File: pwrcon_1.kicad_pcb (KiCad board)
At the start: 2 copper layers, 85.1 x 48 mm, 52 parts, among them J1 CON3, J4 CON3, J5 Conn_01x03_Female, J6 Conn_01x04, J7 CON3, J8 Conn_01x03_Female, Q1 Q_PNP_BEC, U1 LM358, U2 ISOW7841DWE, U3 THVD1500D, U4 SN74LV1T34DBVR, U5 SN74LV1T34DBVR, U6 SN74LV1T34DBVR, U7 MIC5219-3.3YMM

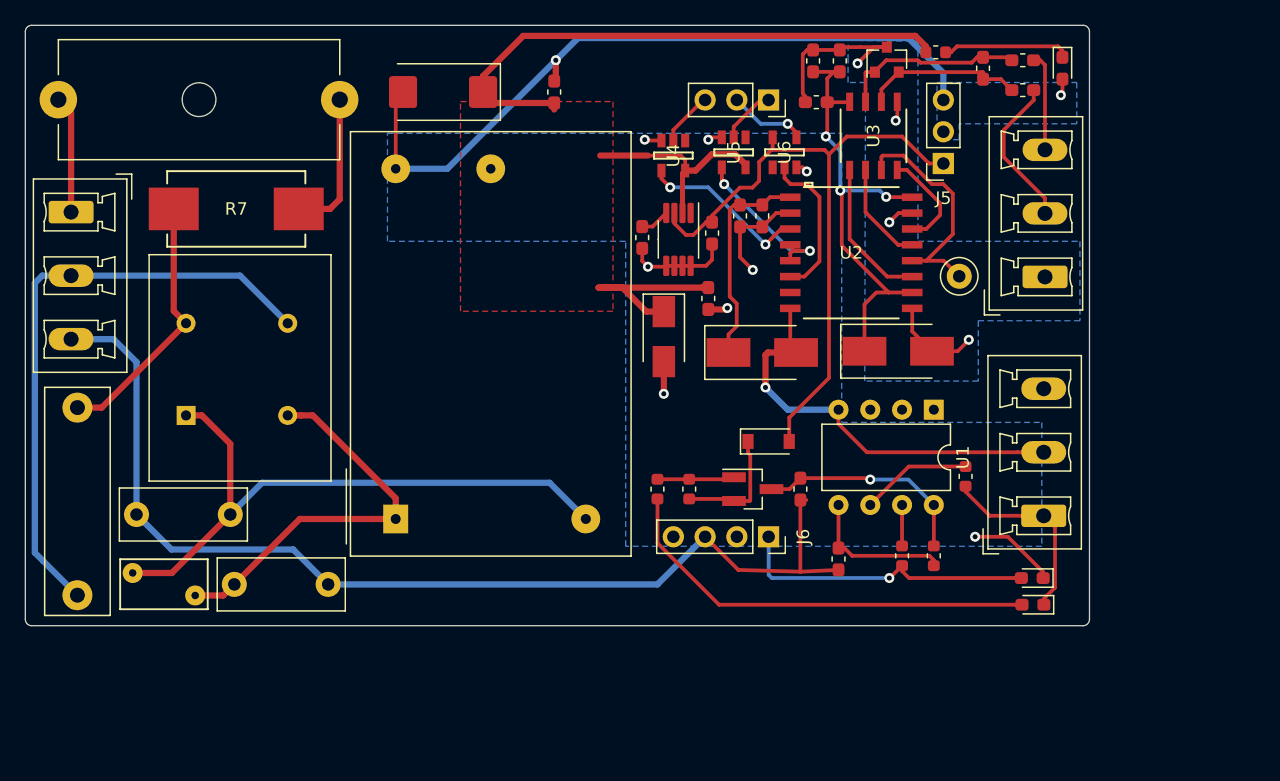
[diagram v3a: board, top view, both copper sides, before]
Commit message: More routing, component footprints finalised and missing ones added into repo
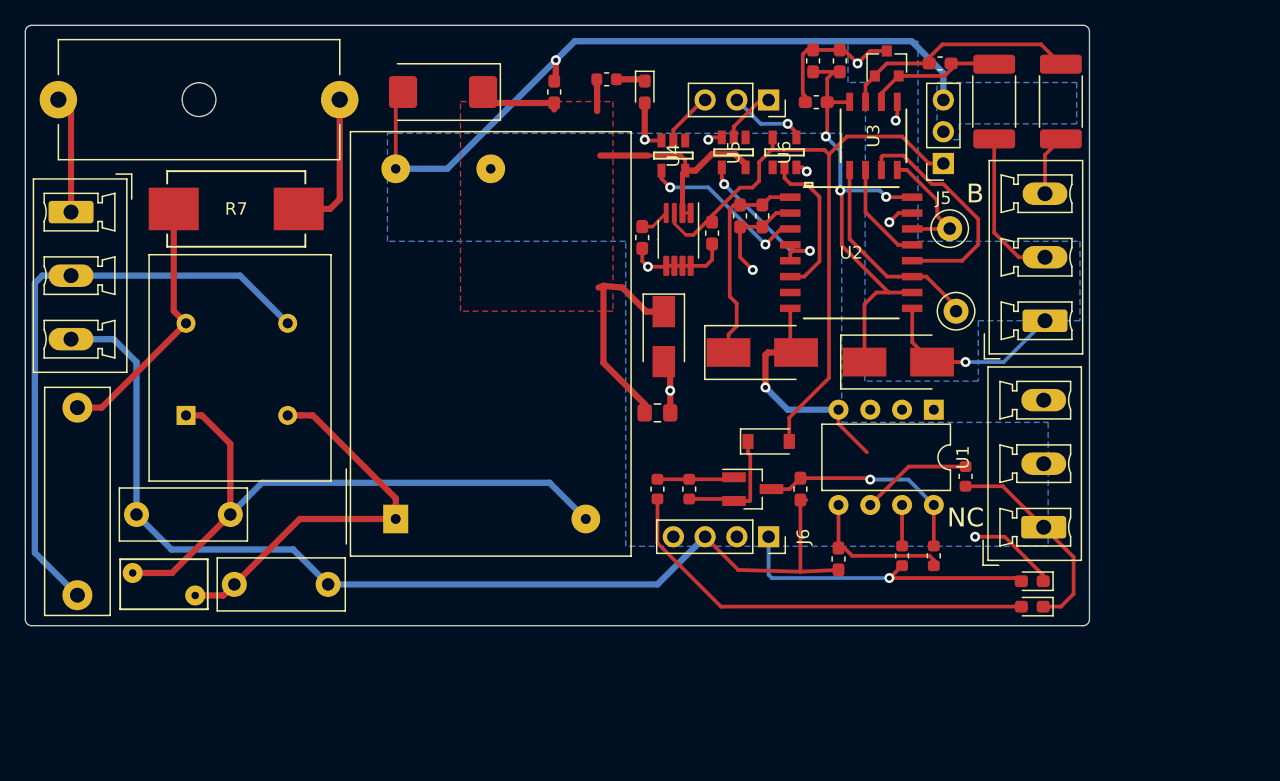
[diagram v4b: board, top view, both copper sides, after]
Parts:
- added TP5: TestPoint, TestPoint:TestPoint_Loop_D1.80mm_Drill1.0mm_Beaded, F.Cu at (175.8, 77.0)
- R10, R11: footprint Resistor_SMD:R_0603_1608Metric_Pad1.05x0.95mm_HandSolder -> Resistor_SMD:R_2512_6332Metric_Pad1.52x3.35mm_HandSolder
- R8: footprint Resistor_SMD:R_0603_1608Metric_Pad1.05x0.95mm_HandSolder -> Resistor_SMD:R_0805_2012Metric_Pad1.15x1.40mm_HandSolder
- moved DR2 33.5 mm to (151.4, 66.0)
- moved R9 26.4 mm to (148.3, 65.0)
- moved R8 10.0 mm to (152.4, 91.7), turned to 0 degrees
- moved R10 4.49 mm to (184.7, 66.8), turned to 90 degrees
- moved J7 3.51 mm to (183.4, 84.3)
- moved R12 3.45 mm to (175.0, 63.8), turned to 180 degrees
- moved TP4 2.81 mm to (176.3, 83.6)
- moved R11 2.46 mm to (179.3, 66.8), turned to 90 degrees
- moved J1 0.91 mm to (183.3, 100.8)
- moved D4 0.86 mm to (171.7, 87.6)
- moved D6 0.30 mm to (170.7, 63.8)
- moved DG1 0.25 mm to (182.4, 105.2)
- moved DR1 0.16 mm to (182.4, 107.2)
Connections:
- U2 pad 11: Net-(U2-Pad11) -> Net-(TP4-Pad1)
- U2 pad 12: Net-(TP4-Pad1) -> Net-(U2-Pad12)
- U3 pad 1: Net-(U2-Pad11) -> Net-(TP4-Pad1)
- U3 pad 3: Net-(TP4-Pad1) -> Net-(U2-Pad12)
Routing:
- net /5VDC: track 79.6 -> 46.3 mm
- net Net-(U2-Pad12): track 0.00 -> 18.8 mm
- net GND: track 212.0 -> 199.6 mm, vias 11 -> 9
- net Net-(U2-Pad11): track 11.8 -> 0.00 mm
- net Net-(DR2-Pad1): track 10.2 -> 2.32 mm
- net GNDA: track 24.9 -> 31.0 mm
- net Net-(D6-Pad1): track 14.8 -> 19.3 mm
- net Net-(J7-Pad3): track 7.84 -> 4.90 mm
- net Net-(TP4-Pad1): track 18.6 -> 16.7 mm
- net Net-(TP5-Pad1): track 8.17 -> 9.89 mm
- net Net-(D6-Pad2): track 12.9 -> 11.3 mm
- net /NC: track 15.3 -> 16.8 mm
- net Net-(DG1-Pad2): track 24.4 -> 25.4 mm
- net Net-(C4-Pad2): track 38.3 -> 39.2 mm
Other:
- board text added: "B"
- board text added: "NC"

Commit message: Aisler fab submit
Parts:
- moved J8 9.01 mm to (152.3, 67.7), turned to 90 degrees
- moved J6 8.95 mm to (152.3, 101.7), turned to 90 degrees
- moved D5 2.64 mm to (158.2, 86.4), turned to 270 degrees
- moved DR2 2.43 mm to (149.4, 64.7)
- moved R9 1.61 mm to (146.7, 64.8), turned to 270 degrees
- moved U5 0.89 mm to (158.5, 71.8)
- moved U4 0.85 mm to (153.9, 71.9)
- moved U6 0.83 mm to (162.6, 71.7)
- moved U2 0.74 mm to (167.9, 79.6)
- moved C7 0.64 mm to (160.8, 76.6)
- moved C8 0.64 mm to (159.0, 76.6)
- moved C10 0.57 mm to (156.8, 77.9)
- moved C11 0.57 mm to (151.2, 78.2)
- moved U7 0.57 mm to (154.1, 78.4)
- moved C2 0.38 mm to (118.6, 105.8)
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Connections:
- J6 pad 3: GND -> (no net)
- J8 pad 2: /RS485_RXD -> /RS485_TXD
- J8 pad 3: /RS485_TXD -> /RS485_RXD
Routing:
- net /RS485_EN: track 4.53 -> 12.9 mm
- net Net-(DG1-Pad2): track 25.4 -> 33.0 mm, vias 1 -> 0
- net /5VDC: track 46.3 -> 53.2 mm
- net Net-(DR1-Pad2): track 34.7 -> 41.0 mm
- net Net-(C2-Pad1): track 31.6 -> 27.2 mm
- net Net-(C7-Pad1): track 17.2 -> 13.1 mm
- net GND: track 199.6 -> 195.9 mm
- net /RS485_RXD: track 6.23 -> 8.04 mm
- net Net-(F1-Pad2): track 11.6 -> 10.0 mm
- net /RS485_TXD: track 4.38 -> 3.48 mm
- net Net-(U2-Pad13): track 8.19 -> 9.01 mm
- net GNDA: track 31.0 -> 30.4 mm
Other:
- board text added: "3V3"
- board text added: "ANA_IN3"
- board text added: "L"
- board text added: "RX"
- board text added: "TX"

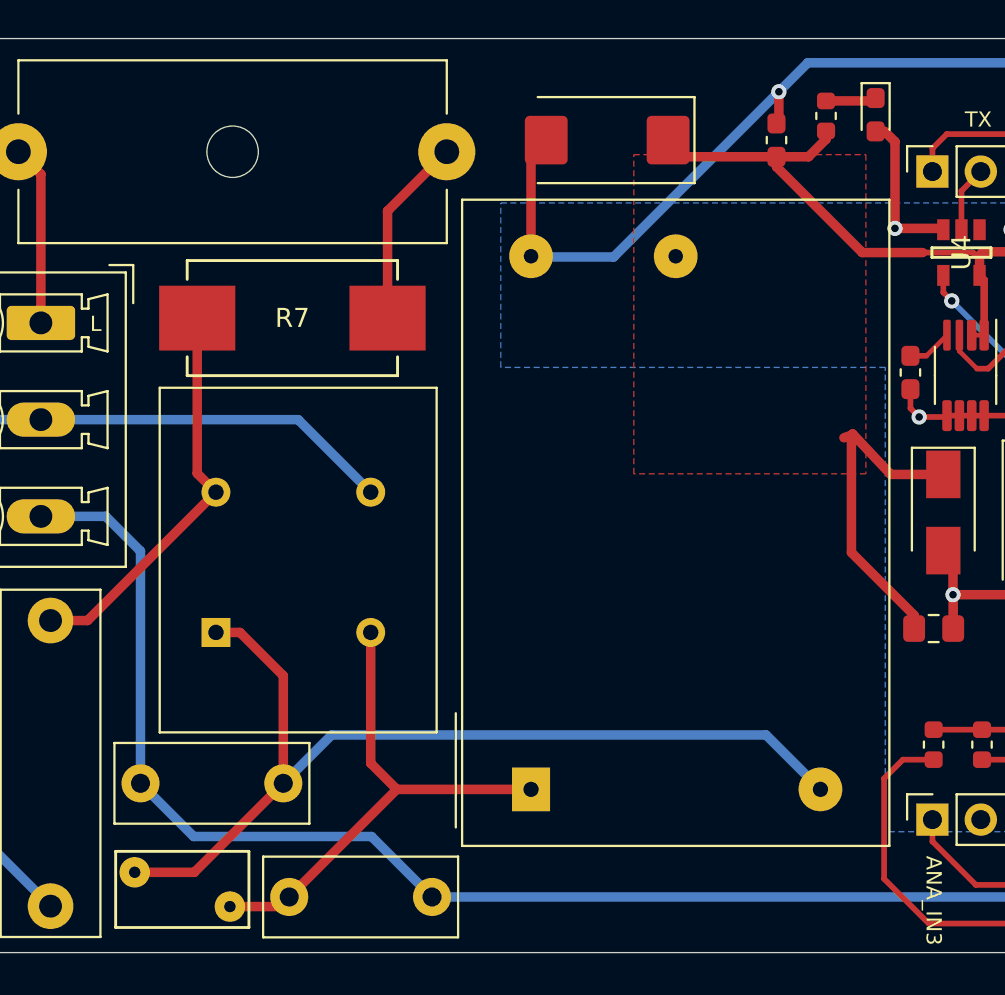
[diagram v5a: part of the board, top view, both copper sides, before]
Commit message: Flipped varistor and led in schematic (no difference to board), cleaned up project/global footprint libraries
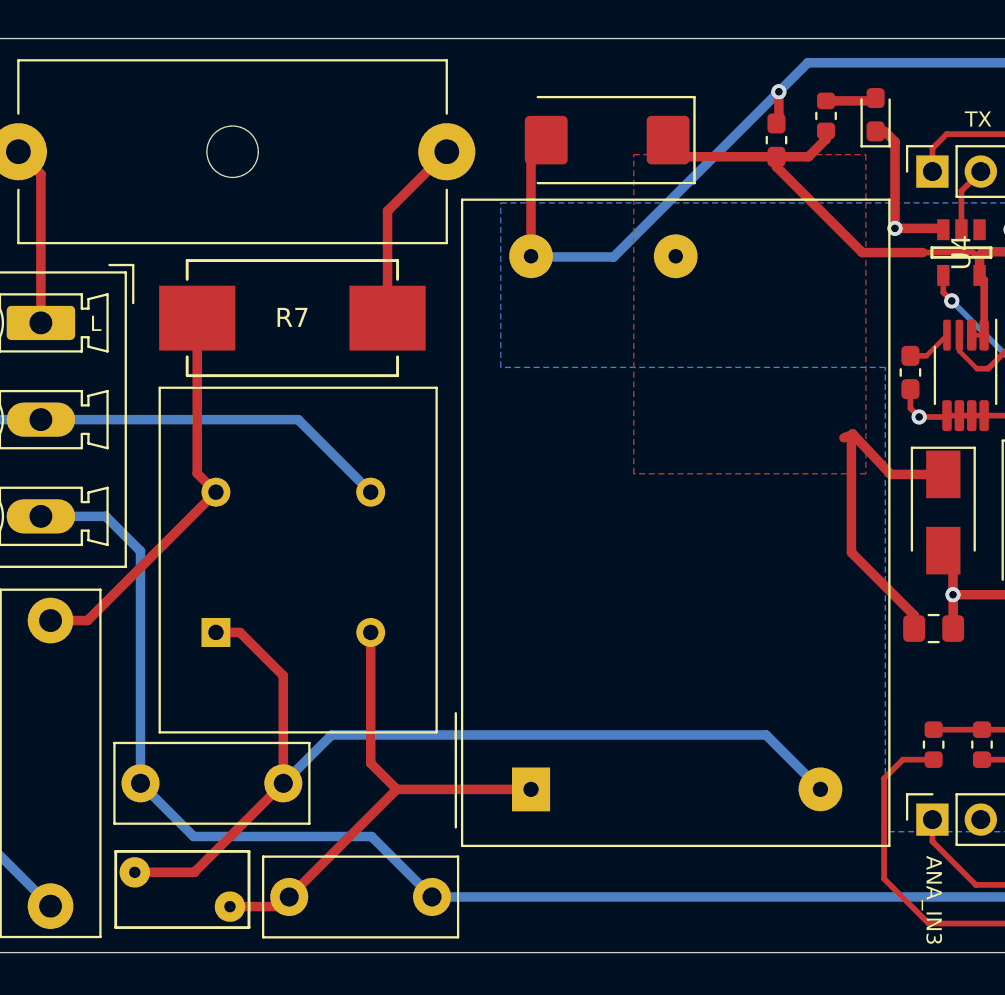
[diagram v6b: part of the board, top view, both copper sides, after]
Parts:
- moved RV1 5.32 mm to (115.4, 106.3), turned to 180 degrees
- turned DR2 to 90 degrees
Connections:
- DR2 pad 1: Net-(DR2-Pad1) -> GND
- DR2 pad 2: GND -> Net-(DR2-Pad2)
- R9 pad 1: Net-(DR2-Pad1) -> Net-(DR2-Pad2)
- RV1 pad 1: Net-(C1-Pad2) -> Net-(C2-Pad1)
- RV1 pad 2: Net-(C2-Pad1) -> Net-(C1-Pad2)
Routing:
- net Net-(DR2-Pad2): track 0.00 -> 2.67 mm
- net Net-(DR2-Pad1): track 2.67 -> 0.00 mm

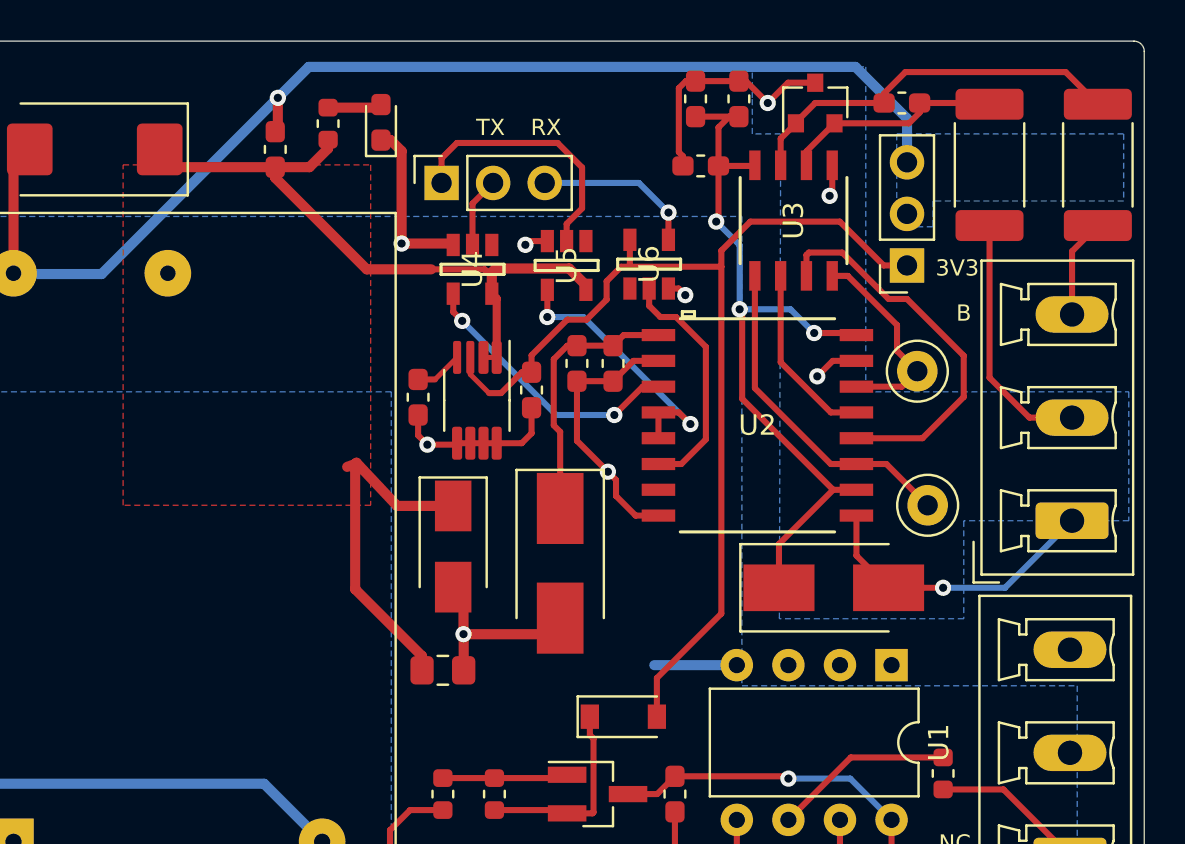
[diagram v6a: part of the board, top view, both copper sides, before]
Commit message: Added missing 5VDC connection to isolator (isow7841dwe) and created new net vcc between isolator and esd/transceiver(thvd1500d). Changed layout.
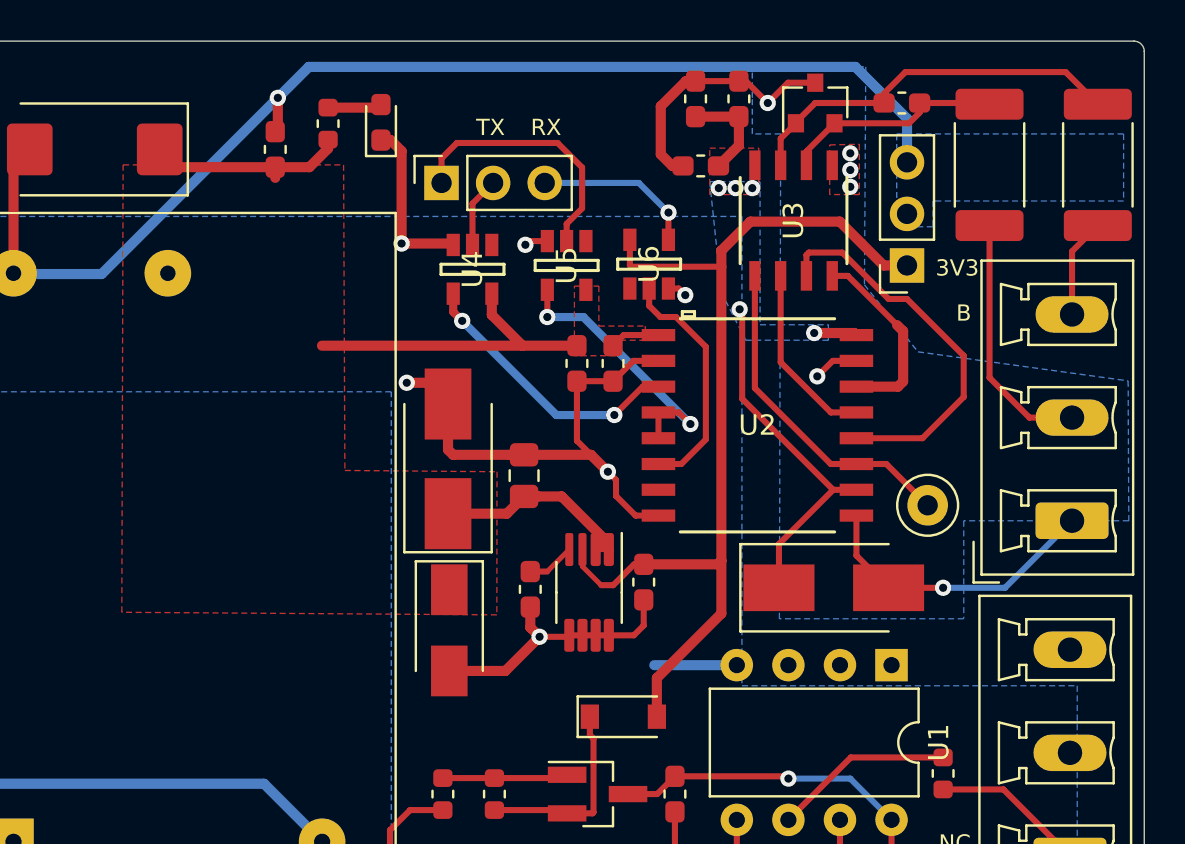
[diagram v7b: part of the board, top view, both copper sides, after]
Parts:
- removed TP5: TestPoint, TestPoint:TestPoint_Loop_D1.80mm_Drill1.0mm_Beaded
- moved C10 11.0 mm to (162.3, 87.4)
- moved C11 11.0 mm to (156.7, 87.7)
- moved U7 11.0 mm to (159.6, 87.9)
- moved R8 10.4 mm to (156.4, 82.1), turned to 90 degrees
- moved D5 7.55 mm to (152.7, 81.3), turned to 90 degrees
- moved D2 4.13 mm to (152.7, 89.7)
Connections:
- net Net-(C4-Pad2) renamed /vcc
- C7 pad 1: Net-(C7-Pad1) -> /5VDC
- C8 pad 1: Net-(C7-Pad1) -> /5VDC
- D5 pad 1: Net-(C7-Pad1) -> /5VDC
- U2 pad 1: Net-(C7-Pad1) -> /5VDC
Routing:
- net /vcc: track 38.8 -> 25.0 mm, vias 3 -> 5
- net Net-(C7-Pad1): track 13.1 -> 0.00 mm
- net /5VDC: track 53.2 -> 41.5 mm
- net GND: track 195.9 -> 205.7 mm
- net /3V3: track 53.4 -> 49.3 mm
- net Net-(U2-Pad14): track 10.2 -> 9.50 mm
- net GNDA: track 30.4 -> 29.9 mm, vias 4 -> 6
- added copper zone on B.Cu, net /vcc
- added copper zone on F.Cu, net /vcc
- added copper zone on F.Cu, net GNDA
